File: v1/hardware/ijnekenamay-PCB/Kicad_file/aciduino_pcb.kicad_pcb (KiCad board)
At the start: 2 copper layers, 151.5 x 95 mm, 39 parts, among them J1 MIDI_OUT, J2 battery, J3 MIDI_IN, SW1 SW_Cherry_MX_1.00u_PCB, SW2 SW_Cherry_MX_1.00u_PCB, SW3 SW_Cherry_MX_1.00u_PCB, SW4 SW_Cherry_MX_1.00u_PCB, SW5 SW_Cherry_MX_1.00u_PCB, SW6 SW_Cherry_MX_1.00u_PCB, U1 6N138

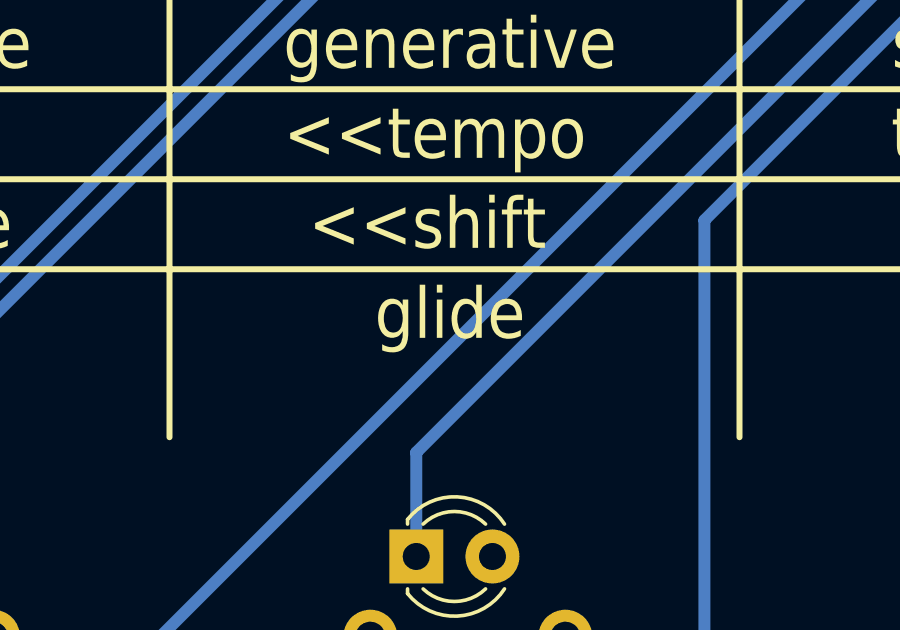
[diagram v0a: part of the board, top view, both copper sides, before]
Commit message: update ijnekenamay's pcb for new tie event panel title
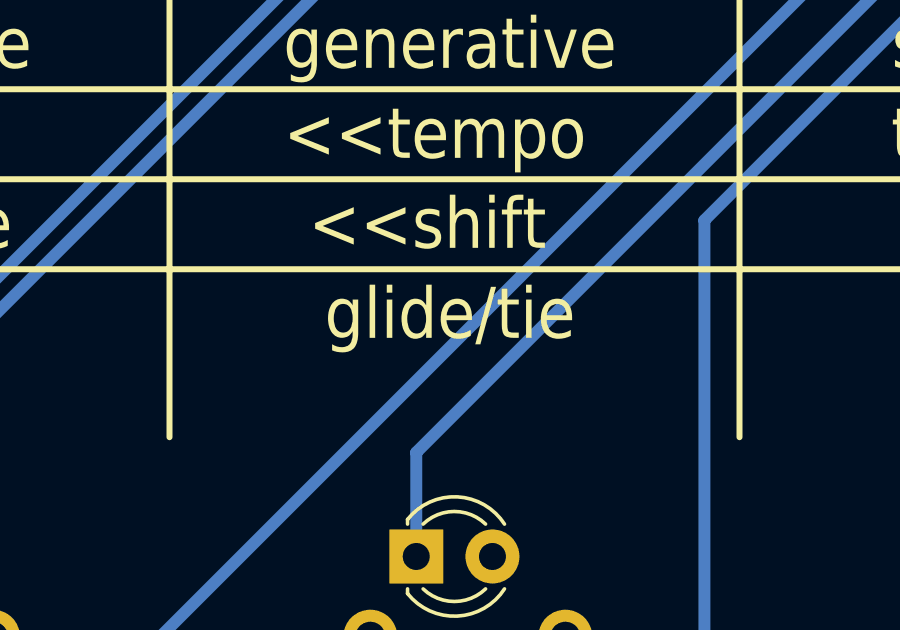
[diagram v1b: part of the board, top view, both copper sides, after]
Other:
- board text added: "glide/tie"
- board text removed: "glide"
